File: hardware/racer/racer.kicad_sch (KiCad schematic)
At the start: 79 parts, among them J1 motor0, J11 UART, J12 JST 2.0 BATT, J2 motor1, J3 motor0, J4 motor1, J5 motor0, J6 motor1, J7 motor0, J8 motor1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

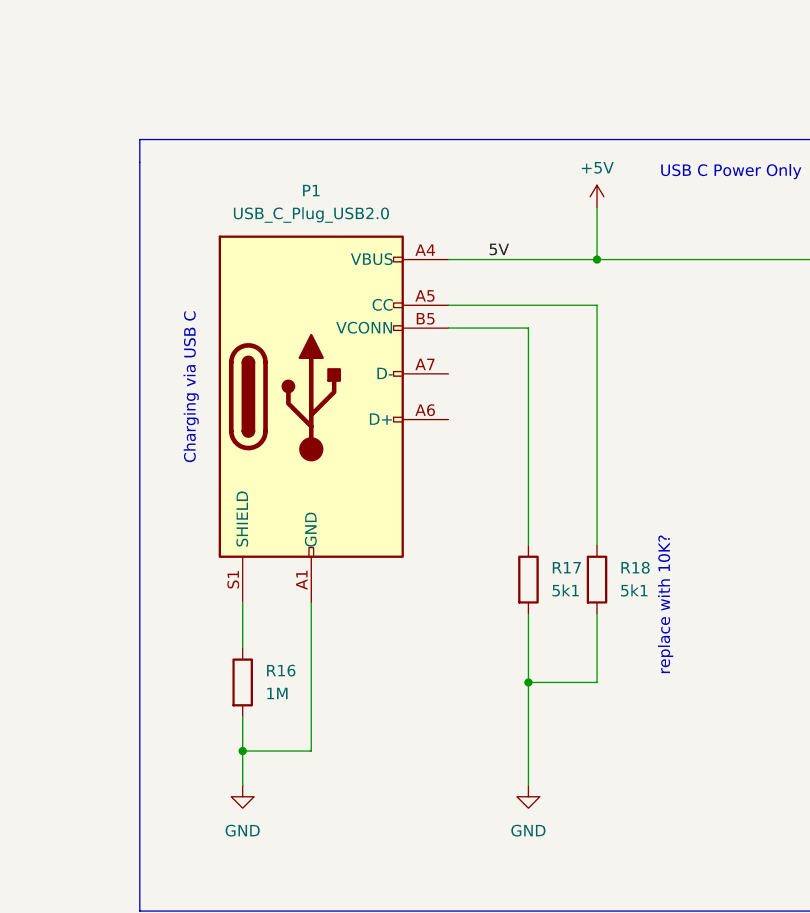
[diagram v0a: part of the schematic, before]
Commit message: Change USB_C_Plug symbol to Connector:USB_C_Receptacle_PowerOnly_6P
The used footprint is 6-pin, so the symbol should have 6 pins to

Signed-off-by: Andreas Heinrich <andreas.heinrich@rwth-aachen.de>
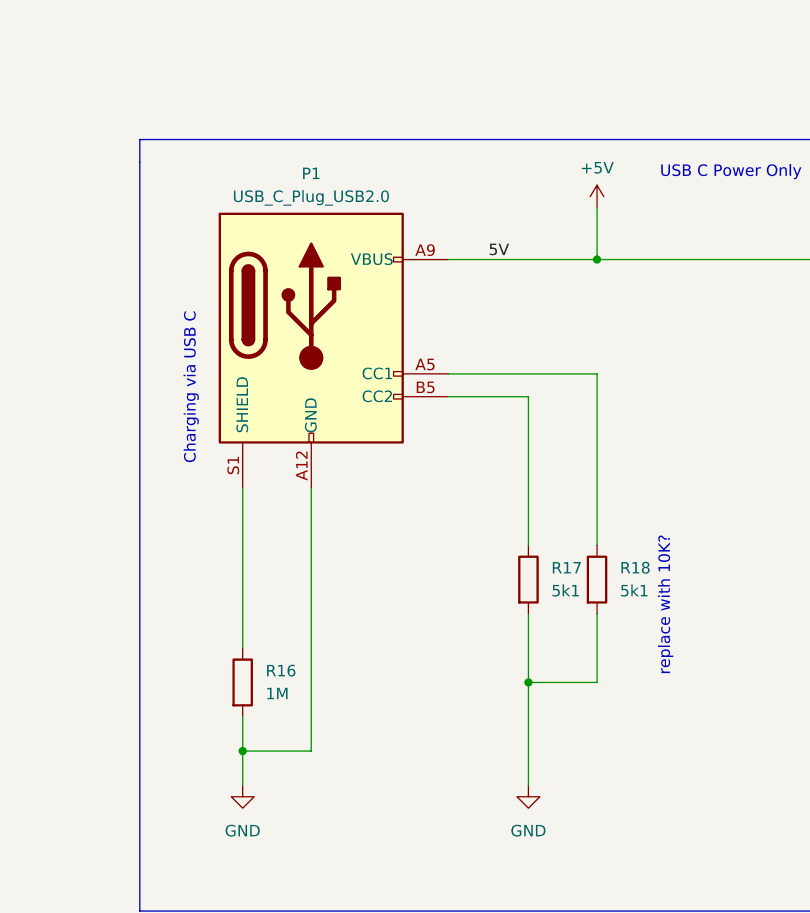
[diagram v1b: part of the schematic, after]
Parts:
- P1: symbol Connector:USB_C_Plug_USB2.0 -> Connector:USB_C_Receptacle_PowerOnly_6P
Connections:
- net +5V: no longer P1.A4 (VBUS), P1.B4 (VBUS)
- net GND: no longer P1.A1 (GND), P1.B1 (GND)
- net at P1.S1 (SHIELD), R16.1: now also P1.S2 (SHIELD)
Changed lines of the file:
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@@
 	)
 	(junction
+		(at 149.225 97.155)
+		(diameter 0)
+		(color 0 0 0 0)
+	)
+	(junction
 		(at 441.325 222.885)
 		(diameter 0)
@@
 	)
 	(junction
-		(at 149.225 97.155)
-		(diameter 0)
-		(color 0 0 0 0)
-	)
-	(junction
 		(at 118.745 249.555)
 		(diameter 0)
@@
 	(wire
 		(pts
-			(xy 117.475 151.765) (xy 117.475 135.255)
-		)
-		(stroke
-			(width 0)
-			(type default)
-		)
-	)
-	(wire
-		(pts
 			(xy 163.195 229.235) (xy 163.195 225.425)
 		)
@@
 		)
 	)
-	(wire
-		(pts
-			(xy 132.715 102.235) (xy 149.225 102.235)
-		)
-		(stroke
-			(width 0)
-			(type default)
-		)
-	)
 	(polyline
 		(pts
@@
 	(wire
 		(pts
+			(xy 117.475 122.555) (xy 117.475 151.765)
+		)
+		(stroke
+			(width 0)
+			(type default)
+		)
+	)
+	(wire
+		(pts
 			(xy 170.815 225.425) (xy 170.815 229.235)
 		)
@@
 	(wire
 		(pts
-			(xy 132.715 97.155) (xy 149.225 97.155)
-		)
-		(stroke
-			(width 0)
-			(type default)
-		)
-	)
-	(wire
-		(pts
 			(xy 283.21 73.025) (xy 283.21 79.375)
 		)
@@
 	(wire
 		(pts
-			(xy 149.225 102.235) (xy 149.225 128.905)
+			(xy 149.225 109.855) (xy 149.225 128.905)
 		)
 		(stroke
@@
 		)
 	)
-	(wire
-		(pts
-			(xy 132.715 104.775) (xy 141.605 104.775)
-		)
-		(stroke
-			(width 0)
-			(type default)
-		)
-	)
 	(polyline
 		(pts
@@
 	(wire
 		(pts
+			(xy 132.715 112.395) (xy 141.605 112.395)
+		)
+		(stroke
+			(width 0)
+			(type default)
+		)
+	)
+	(wire
+		(pts
 			(xy 85.725 291.465) (xy 130.175 291.465)
 		)
@@
 	(wire
 		(pts
+			(xy 132.715 109.855) (xy 149.225 109.855)
+		)
+		(stroke
+			(width 0)
+			(type default)
+		)
+	)
+	(wire
+		(pts
 			(xy 154.305 301.625) (xy 130.175 301.625)
 		)
@@
 	(wire
 		(pts
-			(xy 109.855 135.255) (xy 109.855 140.335)
+			(xy 109.855 122.555) (xy 109.855 140.335)
 		)
 		(stroke
@@
 	(wire
 		(pts
+			(xy 141.605 112.395) (xy 141.605 128.905)
+		)
+		(stroke
+			(width 0)
+			(type default)
+		)
+	)
+	(wire
+		(pts
 			(xy 283.21 120.65) (xy 266.7 120.65)
 		)
@@
 	(wire
 		(pts
-			(xy 141.605 104.775) (xy 141.605 128.905)
-		)
-		(stroke
-			(width 0)
-			(type default)
-		)
-	)
-	(wire
-		(pts
 			(xy 441.325 151.765) (xy 447.675 151.765)
 		)
@@
 	(wire
 		(pts
+			(xy 132.715 97.155) (xy 149.225 97.155)
+		)
+		(stroke
+			(width 0)
+			(type default)
+		)
+	)
+	(wire
+		(pts
 			(xy 480.695 238.125) (xy 485.775 238.125)
 		)
@@
 	)
 	(symbol
-		(lib_id "Connector:USB_C_Plug_USB2.0")
-		(at 117.475 112.395 0)
+		(lib_id "Connector:USB_C_Receptacle_PowerOnly_6P")
+		(at 117.475 104.775 0)
 		(unit 1)
 		(exclude_from_sim no)
@@
 		(fields_autoplaced yes)
 		(property "Reference" "P1"
-			(at 117.475 89.535 0)
+			(at 117.475 87.63 0)
 			(effects
 				(font
@@
 		)
 		(property "Value" "USB_C_Plug_USB2.0"
-			(at 117.475 92.075 0)
+			(at 117.475 90.17 0)
 			(effects
 				(font
@@
 		)
 		(property "Footprint" "kicad_reformed_custom_IC:CUI_UJC-VP-3-SMT-TR"
-			(at 121.285 112.395 0)
+			(at 121.285 102.235 0)
 			(effects
 				(font
@@
 		)
 		(property "Datasheet" "https://www.usb.org/sites/default/files/documents/usb_type-c.zip"
-			(at 121.285 112.395 0)
+			(at 117.475 104.775 0)
 			(effects
 				(font
@@
 			)
 		)
-		(property "Description" ""
-			(at 117.475 112.395 0)
+		(property "Description" "USB Power-Only 6P Type-C Receptacle connector"
+			(at 117.475 104.775 0)
 			(effects
 				(font
@@
 			)
 		)
-		(pin "A1"
-		)
 		(pin "A12"
 		)
-		(pin "A4"
-		)
 		(pin "A5"
 		)
-		(pin "A6"
-		)
-		(pin "A7"
-		)
 		(pin "A9"
 		)
-		(pin "B1"
-		)
 		(pin "B12"
 		)
-		(pin "B4"
-		)
 		(pin "B5"
 		)
@@
 		(pin "S1"
 		)
+		(pin "S2"
+		)
 		(instances
